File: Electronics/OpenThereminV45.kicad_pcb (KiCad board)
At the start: 2 copper layers, 50.5 x 128.5 mm, 107 parts, among them J1 USB_C_Receptacle 12401610E4#2A, J2 Conn_02x03_Odd_Even, J3 Conn_02x05_Odd_Even, P1 10k, P10 BUTTON, P11 A3_PAD, P12 A2_PAD, P13 A1_PAD, P14 A0_PAD, P16 GND, P2 10k, P3 10k, P4 10k, P8 VCC, P9 GND, U1 TTP223, U10 CH340G, U11 LP2985-3.3, U12 MCP4922-E/SL, U2 74HC4060D, U3 74HC4060D, U4 74HC74, U5 HEF4069, U6 MCP4921-E/SN, U7 MCP4922-E/SL, U8 MCP6002T-I/SN, U9 ATmega328P-AU, X1 16MHz, X2 7.3721MHz, Y1 MountPad3, Y2 MountPad3, Y3 PLUG_3_5_SMD SJ-3502-SMT-TR, Y7 PLUG_3_5_SMD SJ-3502-SMT-TR

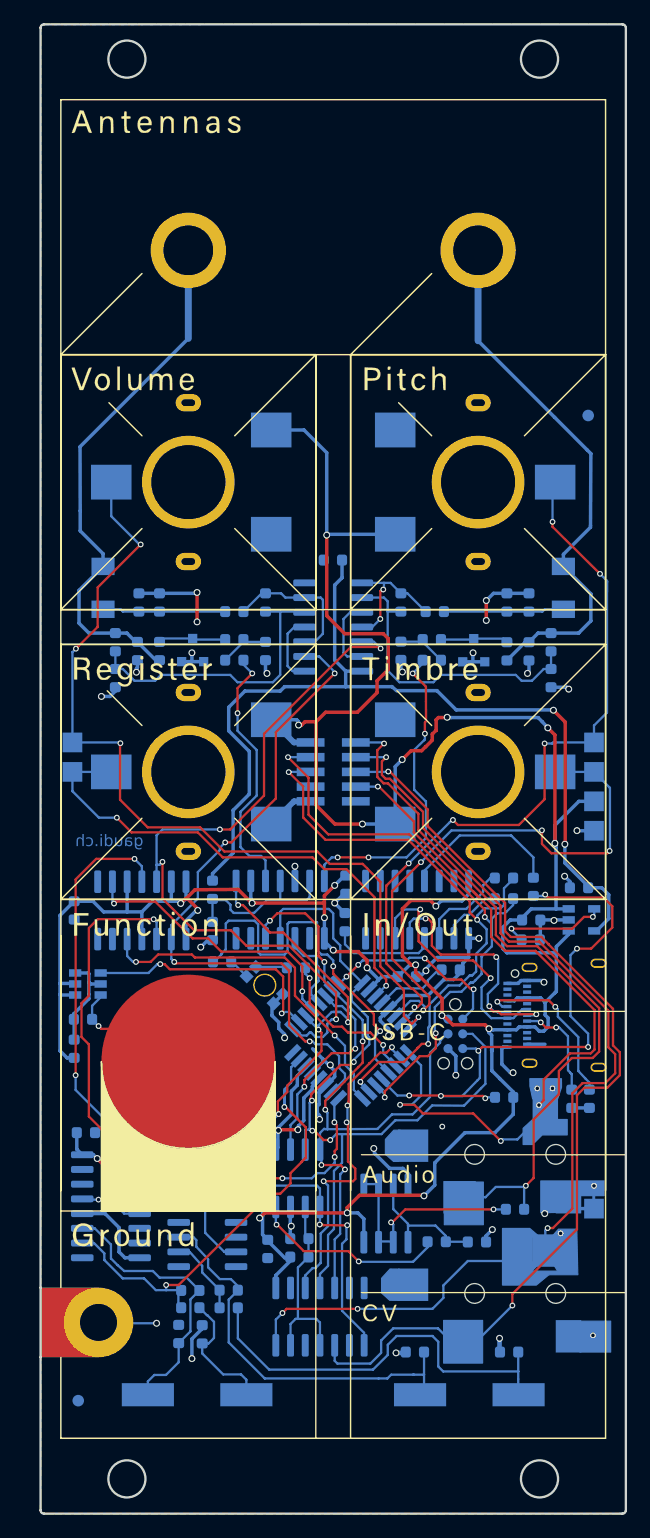
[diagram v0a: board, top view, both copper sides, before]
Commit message: Update schema & layout
- Adjust layout base on JLC capabilities
- Re-do USB layout
- Replace 3.5mm jack, inductor, type-c connector and LED with higher availability option
- Add 5x5mm SN block
- Remove some logos and text for personal preference
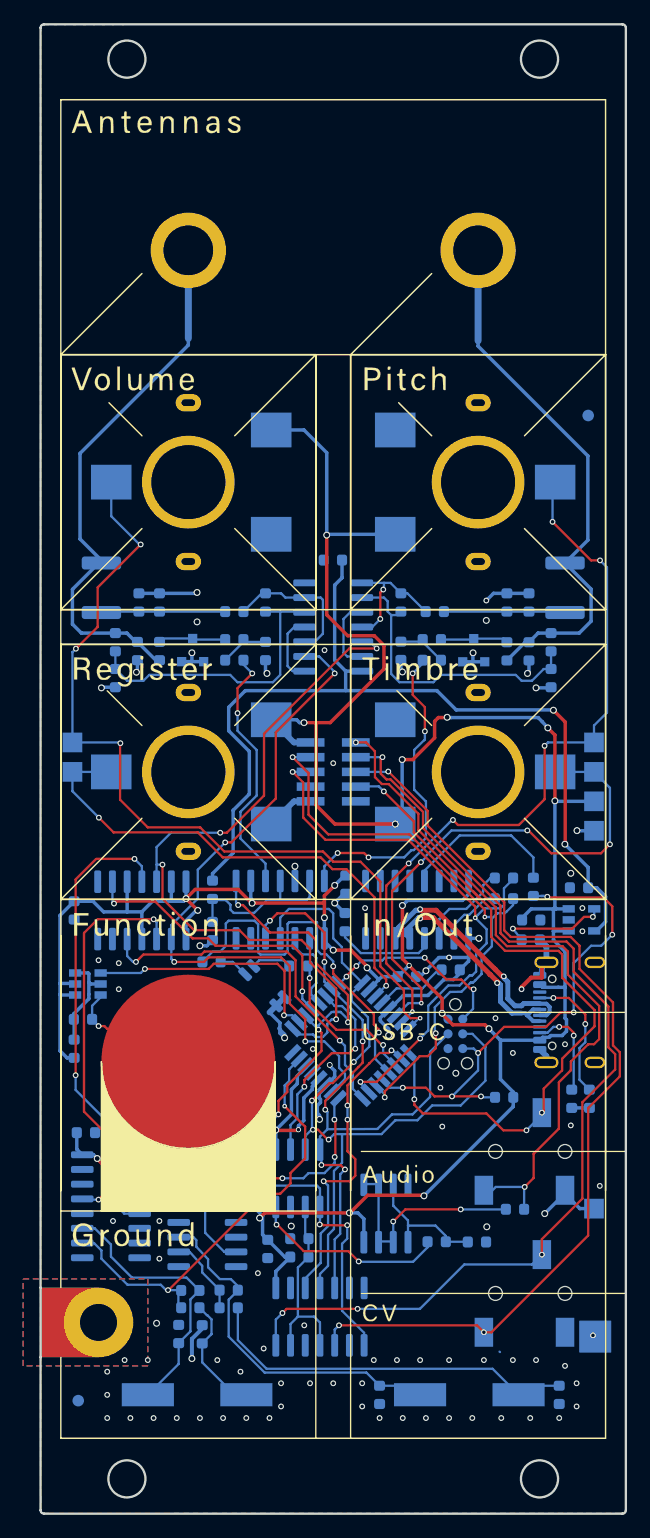
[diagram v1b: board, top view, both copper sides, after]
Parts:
- removed the G*** at (100.0, 154.5)
- removed the G*** at (87.5, 125.8)
- removed the G*** at (100.3, 47.2)
- removed the G*** at (100.7, 61.2)
- removed the G*** at (100.0, 161.9)
- removed J1: USB_C_Receptacle 12401610E4#2A, GaudiLabsFootPrints:USB_C_Receptacle_Amphenol_12401610E4-2A
- removed Y3, Y7: PLUG_3_5_SMD SJ-3502-SMT-TR, GaudiLabsFootPrints:SJ-3502-SMT-TR
- added J4: PJ-320B, Library:XKB_PJ-320B, B.Cu at (122.1, 145.8)
- added J5: PJ-320B, Library:XKB_PJ-320B, B.Cu at (122.1, 133.5)
- added J6: USB_C_Receptacle_USB2.0_16P, Connector_USB:USB_C_Receptacle_GCT_USB4105-xx-A_16P_TopMnt_Horizontal, B.Cu at (121.5, 121.5)
- C1, C10, C2, C3, C7, C8, C9: value 150pF -> 150p
- C12, C5: value 470pF -> 470p
- C13, C23, C24, C25, C26, C27, C28, C6: value 100nF -> 100n
- C14: value 47pF -> 47p
- C15, C16, C34: value 22pF -> 22p
- C17, C18: value 22pF -> 30p
- C29: value 10uF -> 10u
- C4: value not assembled -> ~
- D3: value DualLED 156125RB73000 -> LTST-C235KGKRKT; footprint GaudiLabsFootPrints:WL-SBRW -> LED_SMD:LED_LiteOn_LTST-C235KGKRKT
- L1, L2: value 1mH CC453232A-102KL -> 1mH; footprint GaudiLabsFootPrints:COIL_T -> Inductor_SMD:L_1812_4532Metric
- U10: value CH340G -> CH340C
- X2: value 7.3721MHz -> 7.3728MHz
- Y1: value MountPad3 -> Pitch
- Y2: value MountPad3 -> Volume
- moved C18 5.69 mm to (119.5, 154.5), turned to -90 degrees
- moved C17 4.79 mm to (104.0, 154.5), turned to -90 degrees
- moved R19 0.91 mm to (89.5, 117.1)
- moved R18 0.26 mm to (97.0, 117.5)
- moved L1 0.14 mm to (120.0, 84.9), turned to -90 degrees
- moved L2 0.14 mm to (80.0, 84.9), turned to -90 degrees
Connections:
- net LED_BLUE renamed LED_GREEN
- net Net-(R4-Pad2) renamed VoutA
- D3 pad 2: GND -> Net-(D3-A2)
- D3 pad 4: Net-(D3-Pad4) -> GND
- GROUND1 pad : (no net) -> GND
- J3 pad 8: D- -> unconnected-(J3-Pin_8-Pad8)
- J3 pad 9: D+ -> unconnected-(J3-Pin_9-Pad9)
- R18 pad 1: Net-(D3-Pad4) -> Net-(D3-A2)
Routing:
- net GND: track 130.3 -> 92.4 mm, vias 36 -> 92
- net VCC: track 331.1 -> 315.0 mm
- net RESET: track 50.5 -> 44.8 mm
- net D+: track 23.3 -> 18.8 mm, vias 4 -> 2
- net Net-(D3-A2): track 0.00 -> 3.63 mm
- net Net-(U3-P1): track 34.5 -> 31.3 mm
- net A2: track 48.9 -> 45.7 mm
- net GATE: track 63.7 -> 60.6 mm
- net Net-(J6-CC1): track 14.7 -> 11.6 mm
- net AUDIO: track 62.5 -> 59.4 mm
- net Net-(D3-Pad4): track 2.69 -> 0.00 mm
- net Net-(C18-Pad1): track 35.8 -> 33.3 mm
- net CV1: track 88.6 -> 86.9 mm, vias 5 -> 4
- net EX_CLK: track 40.6 -> 39.0 mm
- net A0: track 66.1 -> 64.6 mm
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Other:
- board text added: "7.3728MHz"
- board text added: "Touch button for 5 seconds to calibrate"
- board text removed: "7.3721MHz"
- board text removed: "gaudi.ch"

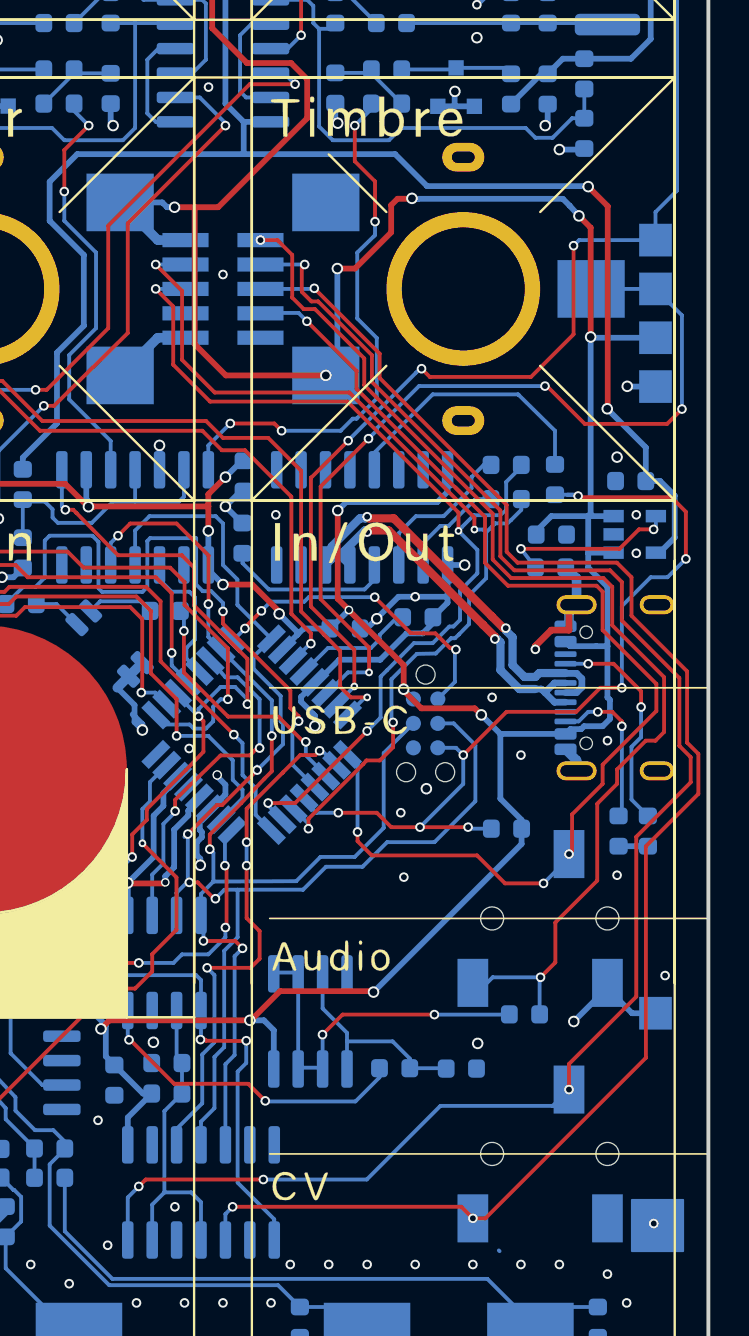
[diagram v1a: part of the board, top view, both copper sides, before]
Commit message: Replace 02x05 pin connector with 02x04
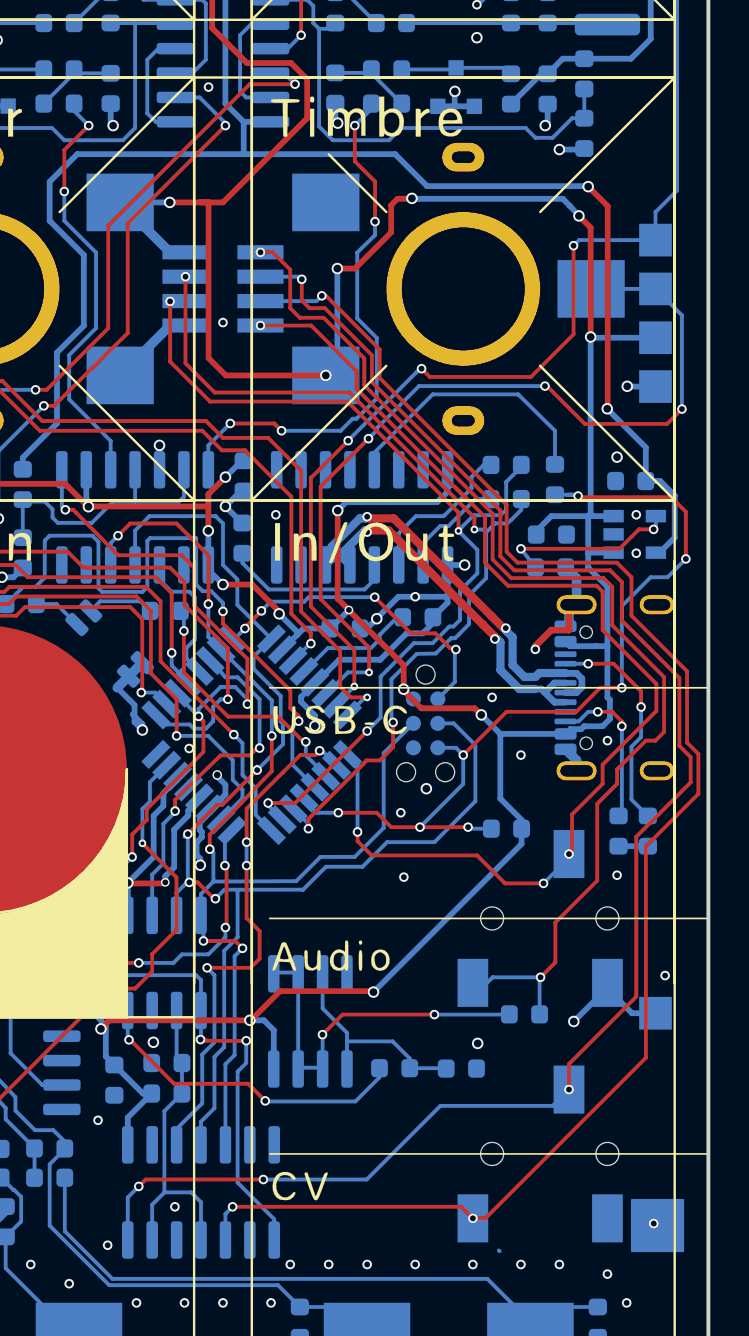
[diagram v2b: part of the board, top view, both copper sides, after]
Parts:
- J3: value Conn_02x05_Odd_Even -> Conn_02x04_Odd_Even; footprint Connector_PinHeader_1.27mm:PinHeader_2x05_P1.27mm_Vertical_SMD -> Connector_PinHeader_1.27mm:PinHeader_2x04_P1.27mm_Vertical_SMD
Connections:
- GROUND1 pad : GND -> (no net)
- J3 pad 8: unconnected-(J3-Pin_8-Pad8) -> GND
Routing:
- net TXD: track 51.6 -> 48.8 mm
- net RXD: track 52.0 -> 49.4 mm
- net CV1: track 86.9 -> 86.2 mm

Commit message: Update schema & layout
- Use SMA as antenna connector
- Replace potentiometers with cheaper & higher avaliability option
- Re-route some of the traces
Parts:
- removed Y1: Pitch, GaudiLabsFootPrints:SMTSOB_M3
- removed Y2: Volume, GaudiLabsFootPrints:SMTSOB_M3
- added J1: Pitch, Connector_Coaxial:SMA_Amphenol_132134-11_Vertical, B.Cu at (112.5, 55.5)
- added J7: Volume, Connector_Coaxial:SMA_Amphenol_132134-11_Vertical, B.Cu at (87.5, 56.0)
- P1, P2, P3, P4: footprint GaudiLabsFootPrints:PS15NV60 -> Library:ALPS_RK09K1130A6S; moved to F.Cu
- moved P1 7.12 mm to (87.5, 82.9), turned to 0 degrees
- moved P2 7.12 mm to (112.5, 82.9), turned to 0 degrees
- moved P3 6.62 mm to (87.5, 94.1), turned to 180 degrees
- moved P4 6.62 mm to (112.5, 94.1), turned to 180 degrees
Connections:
- net Net-(C11-Pad1) renamed /ANT_Volume
- net Net-(C2-Pad1) renamed /ANT_Pitch
- P2 pad 1: GND -> VCC
- P2 pad 3: VCC -> GND
- P3 pad 1: GND -> VCC
- P3 pad 3: VCC -> GND
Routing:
- net A3: track 44.2 -> 52.6 mm
- net /ANT_Pitch: track 46.3 -> 38.1 mm
- net /ANT_Volume: track 46.9 -> 38.7 mm
- net VCC: track 315.5 -> 323.4 mm, vias 26 -> 25
- net A1: track 75.7 -> 71.0 mm, vias 4 -> 3
- net VoutA: track 28.3 -> 25.8 mm, vias 4 -> 2
- net GND: track 92.7 -> 94.4 mm, vias 92 -> 87
- net VO_PITCH: track 63.9 -> 62.3 mm
- net VoutB: track 22.0 -> 20.5 mm
- net VO_VOL: track 59.1 -> 60.3 mm
- net VDD: track 81.5 -> 80.4 mm
- net A2: track 45.7 -> 46.5 mm, vias 4 -> 2
- net A0: track 64.6 -> 64.5 mm, vias 6 -> 5
- added copper zone on B.Cu, net /ANT_Pitch
- added copper zone on B.Cu, net /ANT_Volume

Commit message: Minor changes to the layout
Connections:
- GROUND1 pad : (no net) -> GND
- P1 pad : (no net) -> GND
- P2 pad : (no net) -> GND
- P3 pad : (no net) -> GND
- P4 pad : (no net) -> GND
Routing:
- net VCC: track 323.4 -> 306.7 mm, vias 25 -> 23
- net VDD: track 80.4 -> 76.0 mm
- net VO_PITCH: track 62.3 -> 58.2 mm
- net Net-(U3-Q4): track 44.8 -> 41.8 mm
- net Net-(U10-~{DTR}): track 14.1 -> 11.7 mm
- net A1: track 71.0 -> 69.1 mm
- net Net-(U2-Q5): track 39.9 -> 38.1 mm
- net GND: track 94.4 -> 96.1 mm, vias 87 -> 103
- net A2: track 46.5 -> 48.1 mm, vias 2 -> 3
- net A3: track 52.6 -> 53.8 mm
- net Net-(R1-Pad1): track 11.6 -> 10.8 mm
- net DAC3_CS: track 27.6 -> 26.7 mm, vias 4 -> 2
- net VoutA: track 25.8 -> 24.9 mm
- net D+: track 18.8 -> 19.6 mm
- net CV2: track 82.9 -> 82.2 mm
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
